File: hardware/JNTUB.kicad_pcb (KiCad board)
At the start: 2 copper layers, 47.2 x 101.1 mm, 73 parts, among them J1 PARAM1_CV, J10 B2_HDR_LEFT, J11 B2_HDR_RIGHT, J12 ISP, J2 PARAM2_CV, J3 CLK/TRG, J4 DITTO, J5 OUT1, J6 OUT2, J7 B1_HDR_LEFT, J8 B1_HDR_RIGHT, J9 POWER, Q1 2N3904, Q2 2N3904, Q3 2N3904, U1 ATtiny85, U2 TL074, U3 78L05, U4 79L05

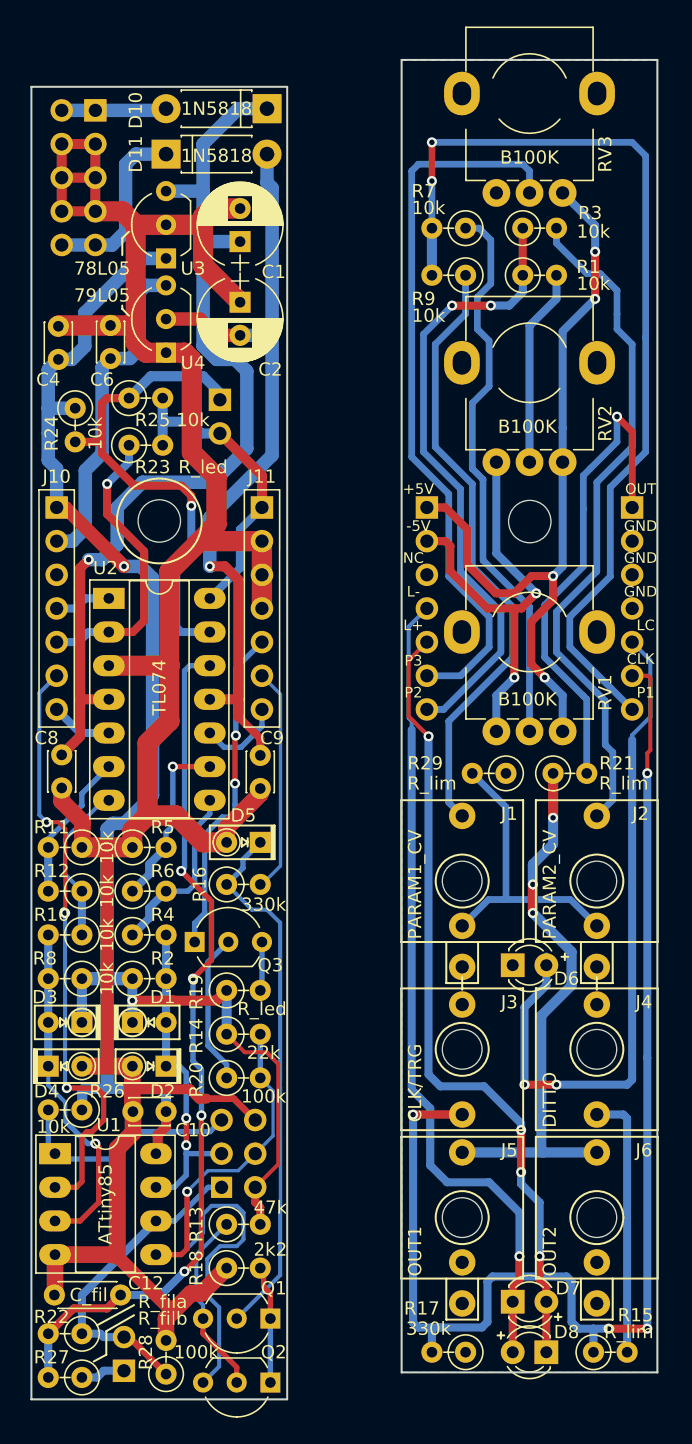
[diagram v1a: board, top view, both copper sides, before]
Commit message: [JNTUB-HW] Some PCB and schematic updates
* Thicker silkscreen on diodes
* Give explicit values to some items
* Update potentiometer schematic symbols
* Fix some symbol names
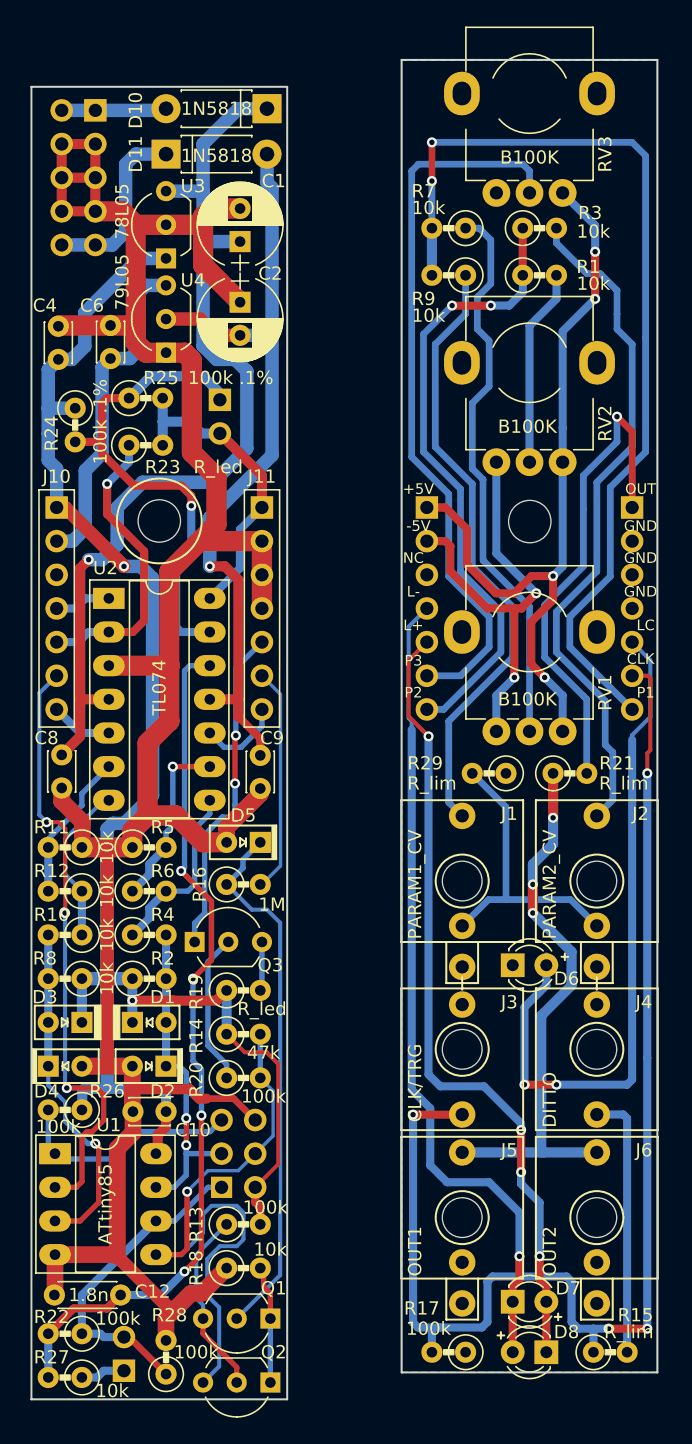
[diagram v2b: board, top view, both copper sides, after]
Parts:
- C1, C2: value 15u -> 22u
- C12: value C_fil -> 1.8n
- D6: value CLK_LED -> LED
- D7: value LED_POS -> LED
- D8: value LED_NEG -> LED
- JP1: value JMP_GATE_OUT -> JMP_UNIPOLAR
- R13: value 47k -> 100k
- R14: value 22k -> 47k
- R16: value 330k -> 1M
- R17: value 330k -> 100k
- R18: value 2k2 -> 10k
- R22: value R_fila -> 100k
- R24, R25: value 10k -> 100k .1%
- R26: value 10k -> 100k
- R27: value R_filb -> 10k

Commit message: [JNTUB-HW] Create SMD version of PCB
Use KiCad scripting API to write a script to turn most
through-hole parts into SMT parts. Will use this to release
two variants of the board.

Had to reroute many traces so that every through hole pad is
connected to traces on the front layer (that way, when all
the through holes are removed, the components are still
connected to traces).
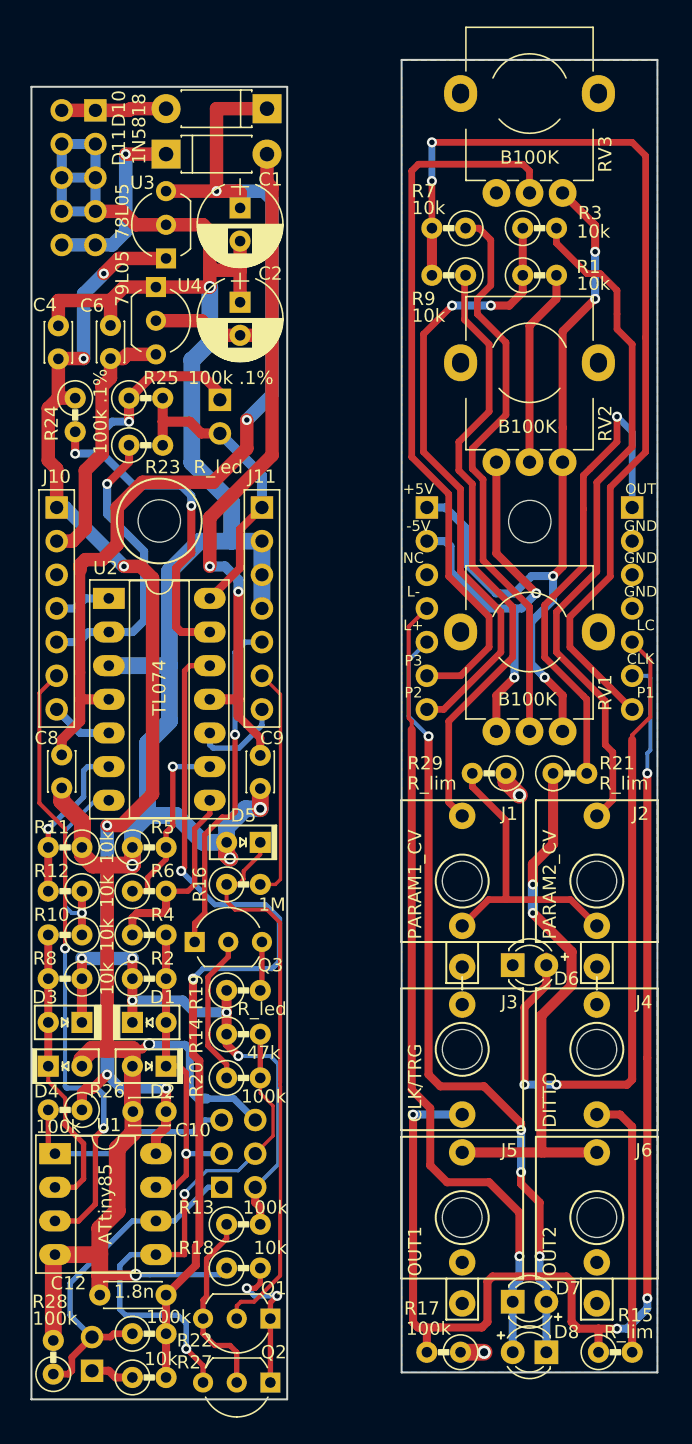
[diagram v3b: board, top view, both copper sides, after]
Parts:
- moved R28 8.51 mm to (197.7, 155.1)
- moved U4 5.01 mm to (205.5, 73.0), turned to 270 degrees
- moved R22 3.81 mm to (203.7, 152.0), turned to 0 degrees
- moved R27 3.81 mm to (203.7, 155.3), turned to 0 degrees
- moved C12 3.43 mm to (206.2, 149.1)
- moved C1 2.54 mm to (211.8, 67.1), turned to 270 degrees
- moved JP2 2.41 mm to (200.7, 154.8)
- moved R24 0.76 mm to (199.4, 81.4)
- moved R15 0.38 mm to (238.9, 153.4)
- moved R17 0.38 mm to (228.5, 153.4)
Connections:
- D3 pad 2: /MainBoard/MCU_ADC2 -> /MainBoard/MCU_ADC3
- D4 pad 1: /MainBoard/MCU_ADC2 -> /MainBoard/MCU_ADC3
- J10 pad 6: /MainBoard/MCU_ADC3 -> /MainBoard/MCU_ADC2
- R10 pad 2: /MainBoard/MCU_ADC2 -> /MainBoard/MCU_ADC3
- R8 pad 2: /MainBoard/MCU_ADC2 -> /MainBoard/MCU_ADC3
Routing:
- net /MainBoard/MCU_ADC3: track 45.7 -> 22.0 mm, vias 3 -> 0
- net /MainBoard/MCU_ADC2: track 27.0 -> 48.6 mm, vias 1 -> 2
- net GNDREF: track 198.9 -> 217.6 mm, vias 0 -> 8
- net /MainBoard/MCU_PB0: track 47.9 -> 40.2 mm, vias 1 -> 2
- net -5V: track 58.4 -> 52.7 mm
- net +12V: track 71.9 -> 75.9 mm, vias 1 -> 2
- net +5V: track 189.0 -> 192.3 mm, vias 6 -> 15
- net Net-(Q1-Pad1): track 8.85 -> 11.6 mm, vias 0 -> 2
- net /MainBoard/MCU_PWM: track 25.3 -> 27.9 mm
- net Net-(R10-Pad1): track 12.7 -> 15.1 mm, vias 0 -> 1
- net Net-(C12-Pad1): track 65.4 -> 67.8 mm, vias 4 -> 2
- net Net-(D5-Pad1): track 40.7 -> 42.6 mm
- net /MainBoard/LED_NEG: track 5.40 -> 4.25 mm
- net Net-(R4-Pad1): track 13.5 -> 14.7 mm
- net /PeripheralBoard/P1_POT: track 42.5 -> 43.5 mm
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- added copper zone on B.Cu, net GNDREF
- removed copper zone on F.Cu, net GNDREF
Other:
- net class Ground: via_dia 1.016 -> 0.9144

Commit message: [JNTUB-HW] PCB now preparable for SMT assembly!
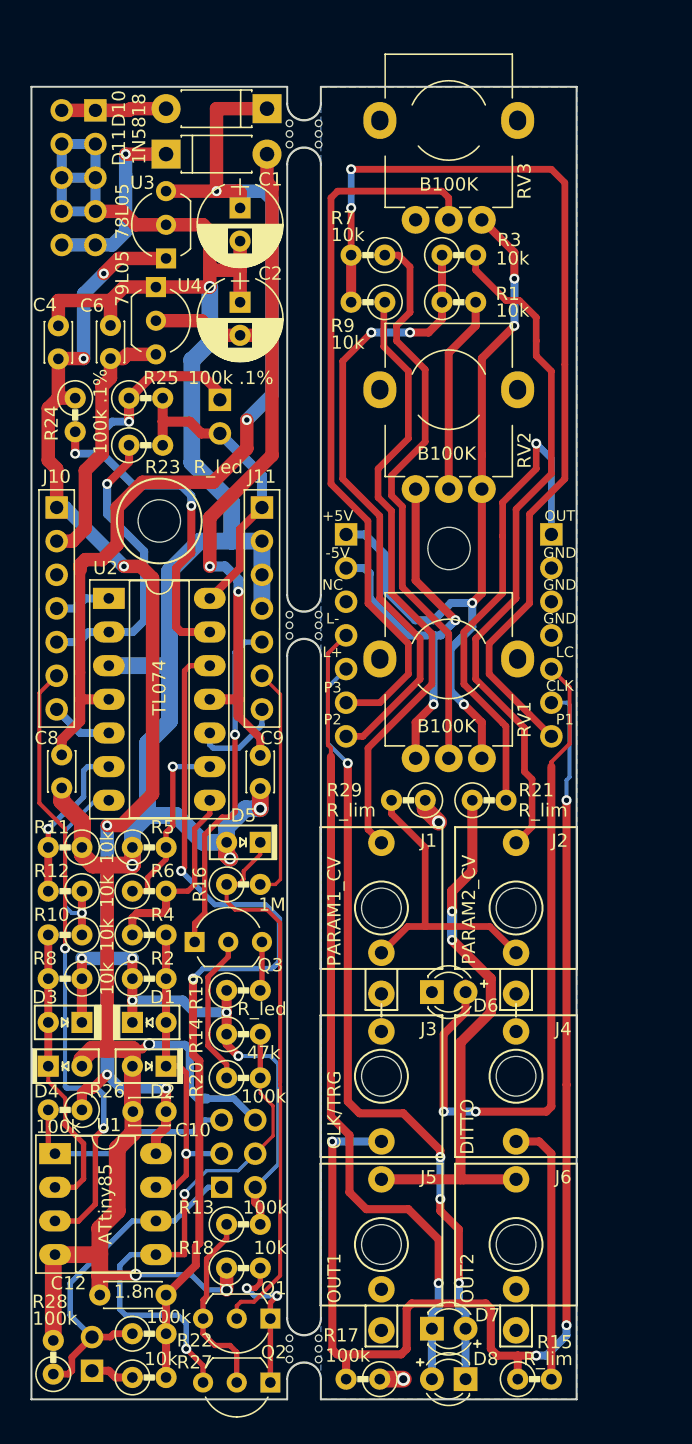
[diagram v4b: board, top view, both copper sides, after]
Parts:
- added mouse-bite-2.54mm-slot: VAL**, Panelization:mouse-bite-2.54mm-slot, F.Cu at (216.7, 98.6)
- added mouse-bite-2.54mm-slot: VAL**, Panelization:mouse-bite-2.54mm-slot, F.Cu at (216.7, 153.2)
- added mouse-bite-2.54mm-slot: VAL**, Panelization:mouse-bite-2.54mm-slot, F.Cu at (216.7, 61.5)
- moved D7 6.43 mm to (226.3, 151.6)
- moved J1 6.43 mm to (222.5, 119.9)
- moved J2 6.43 mm to (232.7, 119.9)
- moved J5 6.43 mm to (222.5, 145.3)
- moved J6 6.43 mm to (232.7, 145.3)
- moved R1 6.43 mm to (227.1, 74.2)
- moved R15 6.43 mm to (232.8, 155.4)
- moved R17 6.43 mm to (222.4, 155.4)
- moved R21 6.43 mm to (229.4, 111.8)
- moved R9 6.43 mm to (222.8, 74.2)
- moved RV2 6.43 mm to (227.6, 80.8)
- moved D6 6.43 mm to (226.3, 126.2)
- moved H1 6.43 mm to (227.6, 92.8)
- moved J7 6.43 mm to (219.8, 91.7)
- moved J8 6.43 mm to (235.3, 91.7)
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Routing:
- net GNDREF: track 217.6 -> 219.5 mm, vias 8 -> 9
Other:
- board size 47.2 x 101.1 mm -> 41.1 x 99.1 mm
- board text added: "CLK/TRG"
- board text added: "DITTO"
- board text added: "OUT1"
- board text added: "OUT2"
- board text added: "PARAM1_CV"
- board text added: "PARAM2_CV"
